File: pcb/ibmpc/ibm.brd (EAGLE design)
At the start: 142 x 56 mm, 23 parts, among them J2 ATX24RH

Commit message: working on ibmpc
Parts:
- removed JP3: (no value), appleii:1X04
- added JP1: (no value), appleii:1X04
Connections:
- net +12V: now also JP1.1; no longer JP3.2
- net GND: now also JP1.2; no longer JP3.1
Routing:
- net N$3: track 0.00 -> 78.4 mm, vias 0 -> 1
- net N$1: track 18.1 -> 70.1 mm
- net +12V: track 36.9 -> 55.5 mm
- net GND: track 0.00 -> 16.9 mm
- net +5V: track 96.7 -> 112.3 mm
- net N$5: track 94.7 -> 92.6 mm
- net N$2: track 78.1 -> 79.8 mm
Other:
- outline, holes or cut-outs redrawn

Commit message: ibmpc done
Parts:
- added C15: 100nF, clock:0805@1
- added JP2: (no value), pinhead:1X03
- added JP3: (no value), pinhead:1X02
- added LED1: (no value), adafruit:LED5MM
- added R1: (no value), adafruit:0207/10
- added TP1, TP2: PTR1PAD1-20, testpad:P1-20
- added U$4: ROCKSW, apricot:ROCKSW
- C13: value (none) -> 100nF; device capacitor-wima:C5B2.5 -> clock:0805@1
- moved U$6 201.1 mm to (3.50, 52.0), turned to 90 degrees
- moved U$5 171.5 mm to (3.50, 18.0), turned to 90 degrees
- moved C13 118.4 mm to (25.2, 48.9), flipped to the bottom
- moved C12 110.0 mm to (25.2, 50.9), turned to 180 degrees
- moved C11 109.9 mm to (25.3, 54.2), turned to 0 degrees
- moved U$1 42.0 mm to (51.0, 41.0)
- moved C8 40.1 mm to (86.9, 31.3)
- moved U$8 40.0 mm to (99.2, 12.0)
- moved C1 40.0 mm to (97.9, 24.0)
- moved C10 40.0 mm to (86.9, 29.6)
- moved C2 40.0 mm to (86.6, 34.3)
- moved C3 40.0 mm to (97.9, 27.4)
- moved C4 40.0 mm to (98.8, 33.9)
- moved C6 40.0 mm to (87.3, 24.1)
- moved C9 40.0 mm to (87.3, 27.4)
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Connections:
- new net N$10: JP2.2, U$4.P$2
- new net N$11: JP2.3, U$4.P$3
- new net N$12: LED1.K, R1.1
- new net N$9: JP2.1, U$4.P$1
- net +12V: now also TP1.TP
- net +3V3: now also C13.2, C15.2, LED1.A; no longer C13.1
- net GND: now also C13.1, C15.1, JP3.2, R1.2, TP2.TP, U$4.P$4, U$4.P$5; no longer C13.2
- net N$3: now also JP3.1
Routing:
- net GND: track 16.9 -> 70.2 mm, vias 0 -> 3
- net +3V3: track 72.0 -> 109.1 mm
- net N$3: track 78.4 -> 103.8 mm, vias 1 -> 2
- net N$9: track 0.00 -> 6.23 mm
- net N$11: track 0.00 -> 6.19 mm
- net +5V: track 112.3 -> 117.8 mm
- net N$12: track 0.00 -> 5.45 mm
- net N$10: track 0.00 -> 5.34 mm
- net N$2: track 79.8 -> 82.4 mm
- net N$7: track 95.4 -> 98.0 mm
- net +12V: track 55.5 -> 57.8 mm
- net N$8: track 95.1 -> 93.3 mm
- net N$5: track 92.6 -> 94.2 mm
- net N$4: track 101.4 -> 102.9 mm
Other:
- board size 142 x 56 mm -> 124 x 56 mm
- board text added: "-5"
- board text added: "3V3"
- board text added: "CRT12"
- board text added: "FAN"
- board text added: "IBM PC PicoPSU Adaptor dekuNukem 2023"
- board text added: "picoRC.com"
- board text removed: "12"
- board text removed: "12\"
- board text removed: "5"
- board text removed: "Apricot PC PicoPSU Adaptor"
- board text removed: "CRT"
- board text removed: "DEDICATED 12V RAIL FOR 5151"
- board text removed: "PSW"
- board text removed: "dekuNukem 2023 picoRC.com"

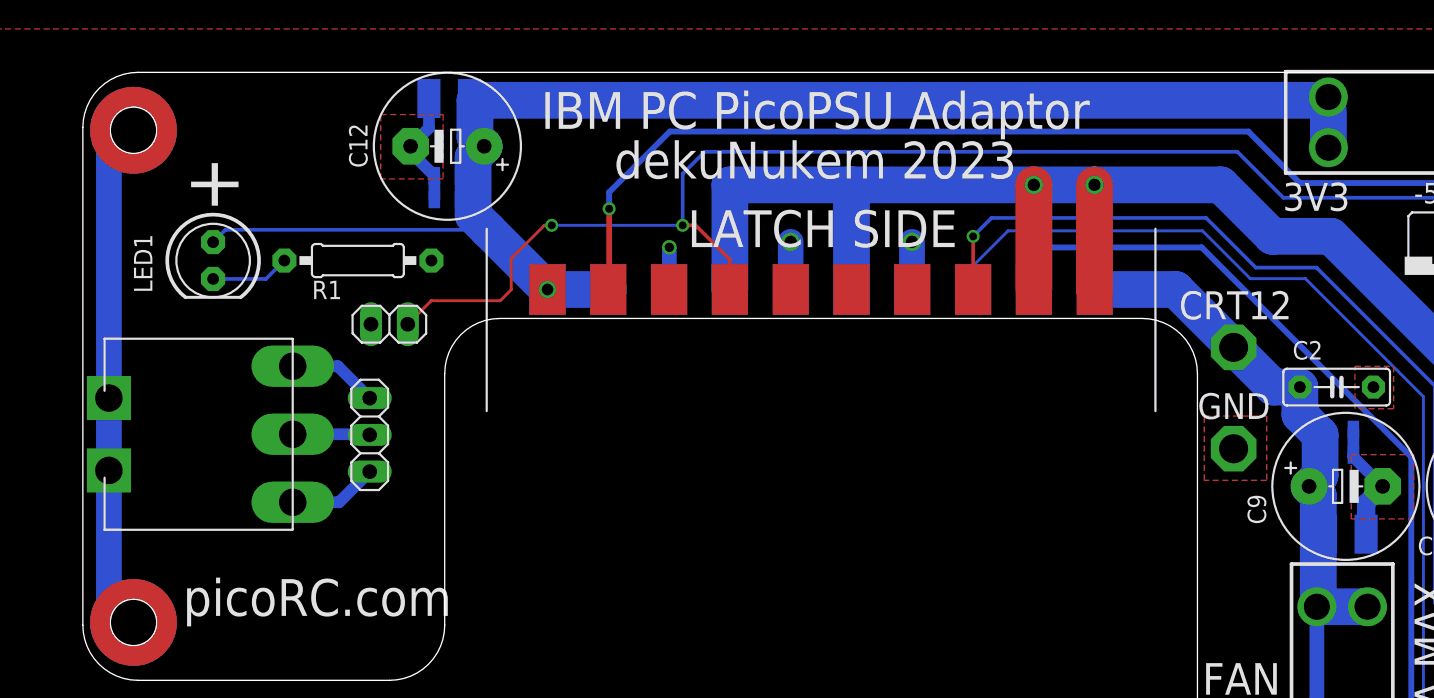
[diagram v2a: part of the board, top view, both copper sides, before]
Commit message: changed ibm switch position
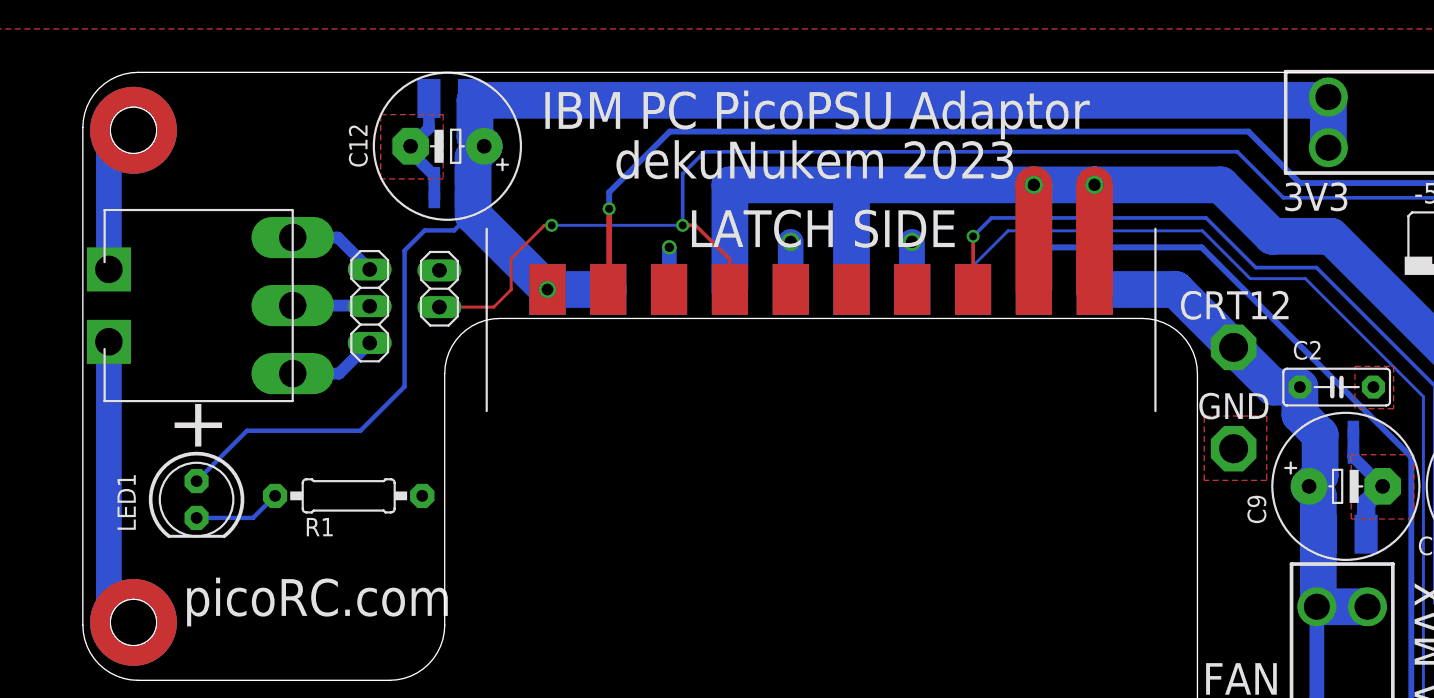
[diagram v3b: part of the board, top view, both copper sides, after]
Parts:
- moved LED1 16.5 mm to (7.86, 26.5)
- moved R1 16.3 mm to (18.4, 26.7)
- moved U$4 8.89 mm to (14.5, 39.9)
- moved JP2 8.89 mm to (19.8, 39.8)
- moved JP3 4.24 mm to (24.6, 41.1), turned to 90 degrees
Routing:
- net +3V3: track 109.1 -> 127.9 mm
- net GND: track 70.2 -> 65.2 mm
- net N$3: track 103.8 -> 101.1 mm
- net N$12: track 5.45 -> 6.06 mm
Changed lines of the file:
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@@
 <text x="79.521" y="32.944" size="1.778" layer="25" rot="R180" align="center">GND</text>
 <text x="79.629" y="39.91" size="1.9304" layer="25" rot="R180" align="center">CRT12</text>
-<text x="9.382" y="48.26" size="3.81" layer="25" distance="35" rot="MR90" align="center">+</text>
+<text x="8.239" y="31.623" size="3.81" layer="25" distance="35" rot="MR90" align="center">+</text>
 <text x="93.091" y="11.716" size="2.1844" layer="25" distance="35" rot="R90" align="center">FUSE 5A MAX</text>
 <wire x1="25" y1="35.19" x2="28.81" y2="39" width="0" layer="20" curve="-90"/>
@@
 <attribute name="NAME" x="21.754" y="47.5295" size="0.8128" layer="26" rot="MR180"/>
 </element>
-<element name="U$4" library="apricot" package="ROCKSW" value="ROCKSW" x="14.5" y="31" smashed="yes"/>
-<element name="JP2" library="pinhead" library_urn="urn:adsk.eagle:library:325" package="1X03" package3d_urn="urn:adsk.eagle:package:22458/2" value="" x="19.817" y="30.956" smashed="yes" rot="R270">
-<attribute name="POPULARITY" value="92" x="19.817" y="30.956" size="1.778" layer="27" rot="R270" display="off"/>
-<attribute name="VALUE" x="16.642" y="34.766" size="1.27" layer="27" rot="R270"/>
-</element>
-<element name="JP3" library="pinhead" library_urn="urn:adsk.eagle:library:325" package="1X02" package3d_urn="urn:adsk.eagle:package:22435/2" value="" x="21.177" y="38.603" smashed="yes" rot="R180">
-<attribute name="POPULARITY" value="98" x="21.177" y="38.603" size="1.778" layer="27" rot="R180" display="off"/>
-<attribute name="VALUE" x="23.717" y="41.778" size="1.27" layer="27" rot="R180"/>
-</element>
-<element name="LED1" library="adafruit" package="LED5MM" value="" x="9" y="43" smashed="yes" rot="R270">
-<attribute name="NAME" x="3.5334" y="44.825" size="1.27" layer="25" ratio="10" rot="R270"/>
-<attribute name="VALUE" x="7.1966" y="39.7996" size="1.27" layer="27" ratio="10" rot="R270"/>
-</element>
-<element name="R1" library="adafruit" package="0207/10" value="" x="19" y="43" smashed="yes">
-<attribute name="NAME" x="15.825" y="40.333" size="1.27" layer="25" ratio="10"/>
-<attribute name="VALUE" x="16.7394" y="42.365" size="1.27" layer="27" ratio="10"/>
+<element name="U$4" library="apricot" package="ROCKSW" value="ROCKSW" x="14.5" y="39.89" smashed="yes"/>
+<element name="JP2" library="pinhead" library_urn="urn:adsk.eagle:library:325" package="1X03" package3d_urn="urn:adsk.eagle:package:22458/2" value="" x="19.817" y="39.846" smashed="yes" rot="R270">
+<attribute name="POPULARITY" value="92" x="19.817" y="39.846" size="1.778" layer="27" rot="R270" display="off"/>
+<attribute name="VALUE" x="16.642" y="43.656" size="1.27" layer="27" rot="R270"/>
+</element>
+<element name="JP3" library="pinhead" library_urn="urn:adsk.eagle:library:325" package="1X02" package3d_urn="urn:adsk.eagle:package:22435/2" value="" x="24.633" y="41.053" smashed="yes" rot="R90">
+<attribute name="POPULARITY" value="98" x="24.633" y="41.053" size="1.778" layer="27" rot="R90" display="off"/>
+<attribute name="VALUE" x="27.808" y="38.513" size="1.27" layer="27" rot="R90"/>
+</element>
+<element name="LED1" library="adafruit" package="LED5MM" value="" x="7.857" y="26.49" smashed="yes" rot="R270">
+<attribute name="NAME" x="2.3904" y="28.315" size="1.27" layer="25" ratio="10" rot="R270"/>
+<attribute name="VALUE" x="6.0536" y="23.2896" size="1.27" layer="27" ratio="10" rot="R270"/>
+</element>
+<element name="R1" library="adafruit" package="0207/10" value="" x="18.365" y="26.744" smashed="yes">
+<attribute name="NAME" x="15.317" y="23.95" size="1.27" layer="25" ratio="10"/>
+<attribute name="VALUE" x="16.1044" y="26.109" size="1.27" layer="27" ratio="10"/>
 </element>
 <element name="TP1" library="testpad" library_urn="urn:adsk.eagle:library:385" package="P1-20" package3d_urn="urn:adsk.eagle:package:27950/1" value="PTR1PAD1-20" x="79.5" y="37" smashed="yes">
@@
 <vertex x="20.574" y="48.641"/>
 </polygon>
-<wire x1="3.5" y1="52" x2="1.8" y2="50.3" width="1.778" layer="16"/>
-<wire x1="1.8" y1="50.3" x2="1.8" y2="33.5" width="1.778" layer="16"/>
-<wire x1="1.8" y1="33.5" x2="1.8" y2="28.5" width="1.778" layer="16"/>
-<wire x1="1.8" y1="28.5" x2="1.8" y2="19.7" width="1.778" layer="16"/>
+<wire x1="1.8" y1="42.39" x2="1.8" y2="50.3" width="1.778" layer="16"/>
+<wire x1="1.8" y1="50.3" x2="3.5" y2="52" width="1.778" layer="16"/>
+<wire x1="1.8" y1="37.39" x2="1.8" y2="19.7" width="1.778" layer="16"/>
 <wire x1="1.8" y1="19.7" x2="3.5" y2="18" width="1.778" layer="16"/>
 </signal>
@@
 <via x="32.1" y="41" extent="1-16" drill="0.8"/>
 <wire x1="86.046" y1="54.296" x2="86.046" y2="54.07" width="2.54" layer="16"/>
-<wire x1="86.046" y1="53.308" x2="86.046" y2="50.796" width="2.54" layer="16"/>
 <wire x1="86.046" y1="54.07" x2="27.088" y2="54.07" width="2.54" layer="16"/>
 <wire x1="36.3" y1="41" x2="32.1" y2="41" width="2.54" layer="16"/>
@@
 <wire x1="27.088" y1="51.53" x2="27.723" y2="50.895" width="2.54" layer="16"/>
 <wire x1="27.723" y1="50.895" x2="26.961" y2="50.133" width="2.54" layer="16"/>
-<wire x1="26.961" y1="46.139" x2="27.9775" y2="45.1225" width="2.54" layer="16"/>
-<wire x1="27.9775" y1="45.1225" x2="32.1" y2="41" width="2.54" layer="16"/>
 <wire x1="26.961" y1="50.133" x2="26.961" y2="46.139" width="2.54" layer="16"/>
 <contactref element="LED1" pad="A"/>
-<wire x1="9" y1="44.27" x2="9.8525" y2="45.1225" width="0.254" layer="16"/>
-<wire x1="9.8525" y1="45.1225" x2="27.9775" y2="45.1225" width="0.254" layer="16"/>
 <wire x1="26.71" y1="54.197" x2="26.71" y2="51.908" width="0.1524" layer="16"/>
 <wire x1="26.71" y1="51.908" x2="27.723" y2="50.895" width="0.1524" layer="16"/>
@@
 <wire x1="26.083" y1="48.863" x2="27.723" y2="50.503" width="0.1524" layer="16"/>
 <wire x1="27.723" y1="50.503" x2="27.723" y2="50.895" width="0.1524" layer="16"/>
-<wire x1="86.046" y1="54.296" x2="86.046" y2="53.308" width="0" layer="19" extent="16-16"/>
+<wire x1="32.1" y1="41" x2="26.961" y2="46.139" width="2.54" layer="16"/>
+<wire x1="27.723" y1="50.895" x2="27.723" y2="47.154" width="0.3048" layer="16"/>
+<wire x1="27.723" y1="47.154" x2="25.654" y2="45.085" width="0.3048" layer="16"/>
+<wire x1="25.654" y1="45.085" x2="23.622" y2="45.085" width="0.3048" layer="16"/>
+<wire x1="22.225" y1="43.688" x2="22.225" y2="34.29" width="0.3048" layer="16"/>
+<wire x1="22.225" y1="34.29" x2="19.177" y2="31.242" width="0.3048" layer="16"/>
+<wire x1="11.339" y1="31.242" x2="7.857" y2="27.76" width="0.3048" layer="16"/>
+<wire x1="23.622" y1="45.085" x2="22.225" y2="43.688" width="0.3048" layer="16"/>
+<wire x1="19.177" y1="31.242" x2="11.339" y2="31.242" width="0.3048" layer="16"/>
+<wire x1="86.046" y1="54.296" x2="86.046" y2="50.796" width="2.54" layer="16"/>
 </signal>
 <signal name="N$2">
@@
 <wire x1="31.882" y1="45.434" x2="29.596" y2="43.148" width="0.2032" layer="1"/>
 <wire x1="29.596" y1="43.148" x2="29.596" y2="40.989" width="0.2032" layer="1"/>
-<wire x1="29.596" y1="40.989" x2="28.834" y2="40.227" width="0.2032" layer="1"/>
-<wire x1="24.071" y1="40.227" x2="22.447" y2="38.603" width="0.2032" layer="1"/>
-<wire x1="28.834" y1="40.227" x2="24.071" y2="40.227" width="0.2032" layer="1"/>
+<wire x1="28.39" y1="39.783" x2="24.633" y2="39.783" width="0.2032" layer="1"/>
+<wire x1="29.596" y1="40.989" x2="28.39" y2="39.783" width="0.2032" layer="1"/>
 </signal>
 <signal name="N$4">
@@
 <contactref element="U$4" pad="P$1"/>
 <contactref element="JP2" pad="1"/>
-<wire x1="14.5" y1="35.7" x2="17.613" y2="35.7" width="0.8128" layer="16"/>
-<wire x1="17.613" y1="35.7" x2="19.817" y2="33.496" width="0.8128" layer="16"/>
+<wire x1="14.5" y1="44.59" x2="17.613" y2="44.59" width="0.8128" layer="16"/>
+<wire x1="17.613" y1="44.59" x2="19.817" y2="42.386" width="0.8128" layer="16"/>
 </signal>
 <signal name="N$10">
 <contactref element="U$4" pad="P$2"/>
 <contactref element="JP2" pad="2"/>
-<wire x1="14.5" y1="31" x2="19.773" y2="31" width="0.8128" layer="16"/>
-<wire x1="19.773" y1="31" x2="19.817" y2="30.956" width="0.8128" layer="16"/>
+<wire x1="14.5" y1="39.89" x2="19.773" y2="39.89" width="0.8128" layer="16"/>
+<wire x1="19.773" y1="39.89" x2="19.817" y2="39.846" width="0.8128" layer="16"/>
 </signal>
 <signal name="N$11">
 <contactref element="U$4" pad="P$3"/>
 <contactref element="JP2" pad="3"/>
-<wire x1="14.5" y1="26.3" x2="17.701" y2="26.3" width="0.8128" layer="16"/>
-<wire x1="17.701" y1="26.3" x2="19.817" y2="28.416" width="0.8128" layer="16"/>
+<wire x1="14.5" y1="35.19" x2="17.701" y2="35.19" width="0.8128" layer="16"/>
+<wire x1="17.701" y1="35.19" x2="19.817" y2="37.306" width="0.8128" layer="16"/>
 </signal>
 <signal name="N$12">
 <contactref element="LED1" pad="K"/>
 <contactref element="R1" pad="1"/>
-<wire x1="9" y1="41.73" x2="12.65" y2="41.73" width="0.254" layer="16"/>
-<wire x1="12.65" y1="41.73" x2="13.92" y2="43" width="0.254" layer="16"/>
+<wire x1="7.857" y1="25.22" x2="11.761" y2="25.22" width="0.3048" layer="16"/>
+<wire x1="11.761" y1="25.22" x2="13.285" y2="26.744" width="0.3048" layer="16"/>
 </signal>
 </signals>

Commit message: cleanup
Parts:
- added U$7: M3_MOUNTING_HOLE, apricot:M3_MOUNTING_HOLE_PACK
- moved C4 0.38 mm to (98.8, 34.3)
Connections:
- net GND: now also U$7.P$1, U$7.P$2
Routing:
- net GND: track 65.2 -> 72.6 mm
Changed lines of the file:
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@@
 <setting verticaltext="up"/>
 </settings>
-<grid distance="5" unitdist="mil" unit="mil" style="lines" multiple="1" display="no" altdistance="1" altunitdist="mil" altunit="mil"/>
+<grid distance="5" unitdist="mil" unit="mm" style="lines" multiple="1" display="no" altdistance="1" altunitdist="mil" altunit="mil"/>
 <layers>
 <layer number="1" name="Top" color="4" fill="1" visible="yes" active="yes"/>
@@
 <rectangle x1="63.632" y1="38.576" x2="67.823" y2="43.529" layer="41"/>
 <rectangle x1="67.823" y1="38.576" x2="72.014" y2="43.529" layer="41"/>
-<text x="16.1986" y="19.7204" size="2.54" layer="25" distance="35" align="center">picoRC.com</text>
+<text x="15.6906" y="18.3234" size="2.54" layer="25" distance="35" align="center">picoRC.com</text>
 <text x="100.076" y="47.657" size="1.4224" layer="25" rot="R180" align="center">G</text>
 <text x="96.52" y="47.657" size="1.4224" layer="25" rot="R180" align="center">-12</text>
@@
 <element name="U$3" library="atx_power_control" package="FUSE_HOLDER_3IN1" value="CAR_FUSE_HOLDER3IN1" x="93.096" y="52.546" smashed="yes" rot="R180"/>
 <element name="C9" library="adafruit" package="E5-10,5" value="" x="87.254" y="27.4" smashed="yes">
-<attribute name="NAME" x="81.7438" y="24.77" size="1.27" layer="25" ratio="10" rot="R90"/>
+<attribute name="NAME" x="81.783" y="27.5148" size="1.27" layer="25" ratio="10" rot="R180"/>
 <attribute name="VALUE" x="84.1298" y="24.1742" size="1.27" layer="27" ratio="10"/>
 </element>
@@
 <attribute name="VALUE" x="94.7978" y="24.1742" size="1.27" layer="27" ratio="10"/>
 </element>
-<element name="C4" library="capacitor-wima" library_urn="urn:adsk.eagle:library:116" package="C5B2.5" package3d_urn="urn:adsk.eagle:package:5426/1" value="" x="98.811" y="33.877" smashed="yes">
-<attribute name="NAME" x="95.382" y="35.655" size="1.27" layer="25" ratio="10"/>
-<attribute name="POPULARITY" value="10" x="92.207" y="27.654" size="1.778" layer="27" display="off"/>
-<attribute name="VALUE" x="96.779" y="31.083" size="1.27" layer="27" ratio="10"/>
+<element name="C4" library="capacitor-wima" library_urn="urn:adsk.eagle:library:116" package="C5B2.5" package3d_urn="urn:adsk.eagle:package:5426/1" value="" x="98.811" y="34.258" smashed="yes">
+<attribute name="NAME" x="95.382" y="36.036" size="1.27" layer="25" ratio="10"/>
+<attribute name="POPULARITY" value="10" x="92.207" y="28.035" size="1.778" layer="27" display="off"/>
+<attribute name="VALUE" x="96.779" y="31.464" size="1.27" layer="27" ratio="10"/>
 </element>
 <element name="C7" library="clock" package="0805@1" value="100nF" x="97.922" y="29.559" smashed="yes" rot="MR0">
@@
 <attribute name="TP_SIGNAL_NAME" value="" x="79.5" y="30" size="1.778" layer="27" display="off"/>
 </element>
+<element name="U$7" library="apricot" package="M3_MOUNTING_HOLE_PACK" value="M3_MOUNTING_HOLE" x="80" y="22.75" smashed="yes"/>
 </elements>
 <signals>
@@
 <wire x1="1.8" y1="37.39" x2="1.8" y2="19.7" width="1.778" layer="16"/>
 <wire x1="1.8" y1="19.7" x2="3.5" y2="18" width="1.778" layer="16"/>
+<contactref element="U$7" pad="P$1"/>
+<contactref element="U$7" pad="P$2"/>
+<wire x1="79.5" y1="30" x2="79.5" y2="23.5" width="1.778" layer="16"/>
+<wire x1="79.5" y1="23.5" x2="80" y2="22.75" width="1.778" layer="16"/>
 </signal>
 <signal name="+5V">
@@
 <contactref element="C7" pad="2"/>
 <contactref element="C5" pad="2"/>
-<wire x1="96.271" y1="33.877" x2="96.271" y2="28.289" width="2.54" layer="16"/>
+<wire x1="96.271" y1="34.258" x2="96.271" y2="28.289" width="2.54" layer="16"/>
 <wire x1="96.271" y1="28.289" x2="95.382" y2="27.4" width="2.54" layer="16"/>
 <wire x1="95.382" y1="27.4" x2="96.017" y2="26.765" width="2.54" layer="16"/>
@@
 <wire x1="97.442" y1="19.083" x2="100.942" y2="19.083" width="2.54" layer="16"/>
 <wire x1="96.271" y1="34.639" x2="86.238" y2="44.672" width="2.54" layer="16"/>
-<wire x1="96.271" y1="34.639" x2="96.271" y2="33.877" width="2.54" layer="16"/>
+<wire x1="96.271" y1="34.639" x2="96.271" y2="34.258" width="2.54" layer="16"/>
 <wire x1="78.618" y1="48.228" x2="82.174" y2="44.672" width="2.54" layer="16"/>
 <wire x1="82.174" y1="44.672" x2="86.238" y2="44.672" width="2.54" layer="16"/>
-<wire x1="96.271" y1="33.877" x2="97.022" y2="33.126" width="0.508" layer="16"/>
-<wire x1="97.022" y1="33.126" x2="97.022" y2="31.337" width="0.508" layer="16"/>
+<wire x1="96.271" y1="34.258" x2="97.022" y2="33.507" width="0.508" layer="16"/>
+<wire x1="97.022" y1="33.507" x2="97.022" y2="31.337" width="0.508" layer="16"/>
 <wire x1="97.022" y1="31.337" x2="97.022" y2="29.559" width="0.508" layer="16"/>
 <wire x1="97.022" y1="29.559" x2="97.022" y2="29.04" width="0.508" layer="16"/>
